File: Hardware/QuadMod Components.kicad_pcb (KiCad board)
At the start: 4 copper layers, 70.6 x 100 mm, 119 parts, among them J1 Conn_01x08_Pin, J2 Conn_01x08_Pin, J3 Conn_01x08_Pin, J4 Conn_01x08_Pin, J5 Eurorack_10_pin_power, J6 USB_B_Micro, J7 Prog_Header, J8 Extra_Outs, U1 LD1117-3.3-4Tab, U2 STM32H563VIT, U3 TL072, U4 MCP6004, U5 TPS561201, U6 MCP6004, U7 MCP6002-xSN, U8 STF202-22T1G, U9 AK4619VN, Y1 8MHz 20pF

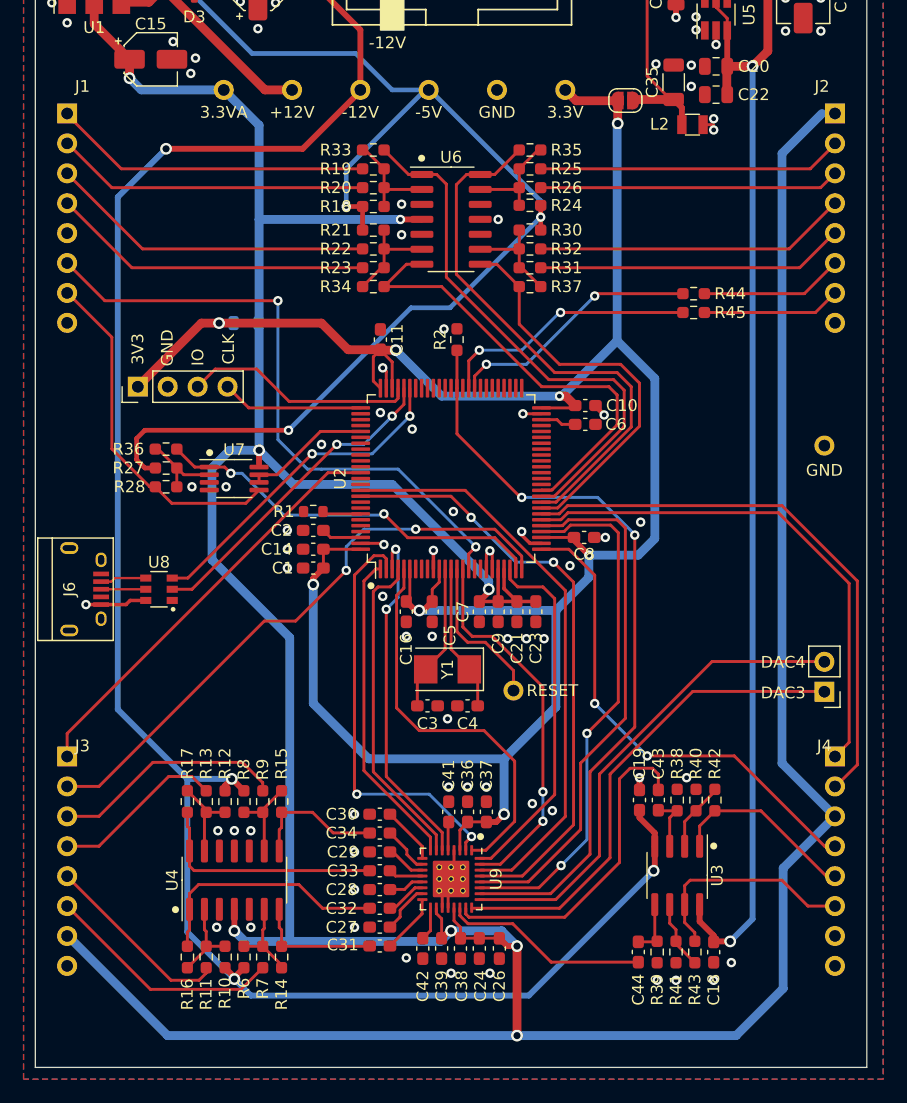
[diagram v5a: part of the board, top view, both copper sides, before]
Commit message: Started adding additional clock LED
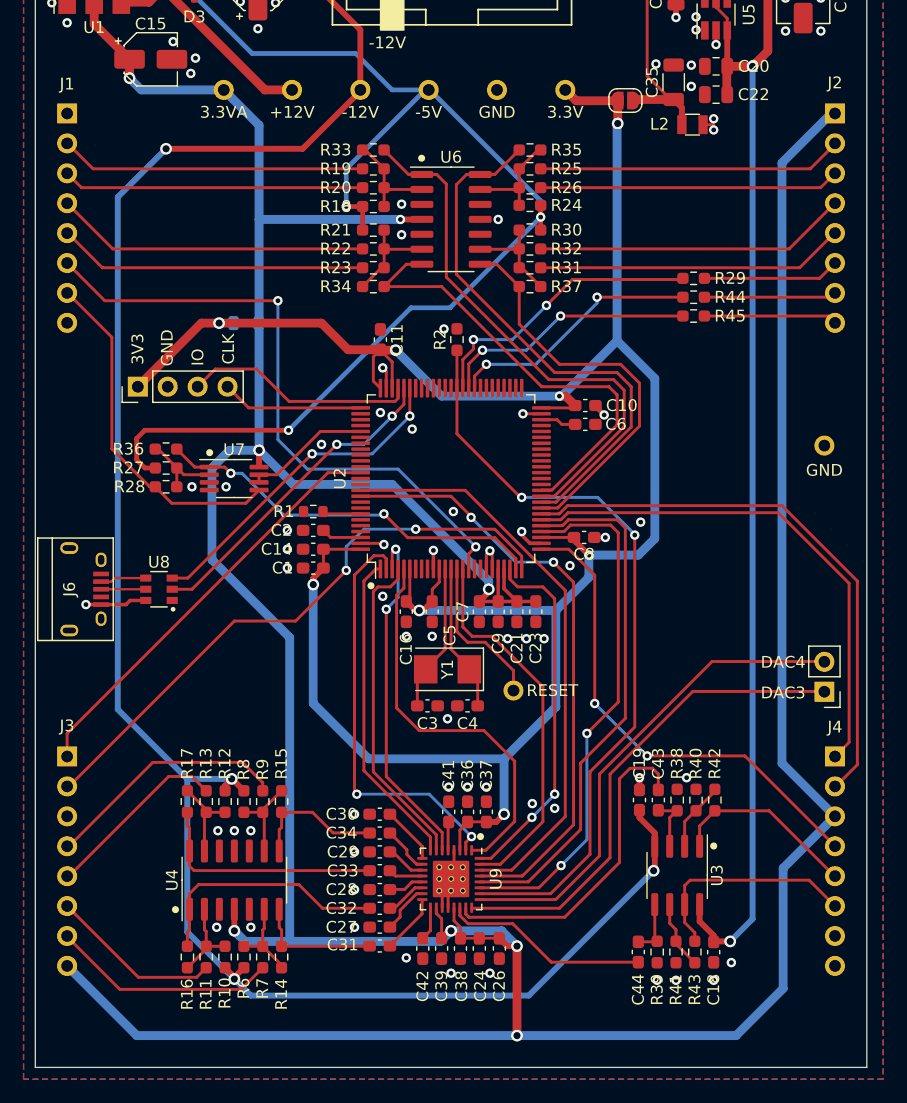
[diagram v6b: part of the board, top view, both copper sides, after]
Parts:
- added R29: 1k, Resistor_SMD:R_0603_1608Metric_Pad0.98x0.95mm_HandSolder, F.Cu at (155.9, 83.0)
- moved R44 0.30 mm to (155.9, 84.6)
- moved R45 0.30 mm to (155.9, 86.2)
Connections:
- J1 pad 1: /LFO_BASEFREQ_CV -> GND
- J1 pad 2: /LFO_BASEFREQ_POT -> /LFO_BASEFREQ_CV
- J1 pad 3: /DLY_FILTER_CV -> /LFO_BASEFREQ_POT
- J1 pad 4: /DLY_FILTER_POT -> /DLY_FILTER_CV
- J1 pad 5: GND -> /DLY_FILTER_POT
- J2 pad 1: +3.3VA -> GND
- J2 pad 6: /DELAY_LED -> /CLOCKED_LED
- J2 pad 7: /FX_LED -> /DELAY_LED
- J2 pad 8: GND -> /FX_LED
- J3 pad 3: /IN4 -> GND
- J3 pad 4: /IN3 -> /IN4
- J3 pad 5: /IN2 -> /IN3
- J3 pad 6: /IN1 -> /IN2
- J3 pad 7: +3.3VA -> /IN1
- J3 pad 8: GND -> +3.3VA
- U2 pad 61: unconnected-(U2-PD14-Pad61) -> /Clocked_Led_Out
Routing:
- net /Clocked_Led_Out: track 0.00 -> 24.4 mm, vias 0 -> 2
- net /CLOCKED_LED: track 0.00 -> 11.6 mm
- net /IN2: track 16.2 -> 14.7 mm
- net /LFO_BASEFREQ_CV: track 27.1 -> 26.0 mm
- net /DLY_FILTER_CV: track 27.8 -> 26.7 mm
- net /IN3: track 14.8 -> 15.8 mm
- net /LFO_BASEFREQ_POT: track 26.6 -> 25.6 mm
- net /IN4: track 19.9 -> 21.0 mm
- net /DLY_FILTER_POT: track 27.4 -> 26.3 mm
- net /IN1: track 20.3 -> 19.3 mm
- net /DELAY_LED: track 12.2 -> 11.2 mm
- net /SAI2_SD_B: vias 0 -> 2
- net /SAI2_SD_A: vias 2 -> 0

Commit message: Clean up of schematics and PCBS
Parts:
- added J9: Test_Outs, Connector_PinHeader_2.54mm:PinHeader_1x02_P2.54mm_Vertical, F.Cu at (104.1, 94.8)
- added TP9: TestPoint, Custom_Footprints:1mm_Test_Point, F.Cu at (102.7, 147.1)
- moved C15 2.00 mm to (109.8, 66.4), turned to -90 degrees
- moved J8 1.03 mm to (167.9, 118.6)
- moved R5 0.10 mm to (114.2, 53.5)
- moved C27 0.05 mm to (129.2, 138.1)
- moved C31 0.05 mm to (129.2, 139.7)
- moved C32 0.05 mm to (129.2, 136.5)
- moved C28 0.05 mm to (129.2, 134.9)
- moved C29 0.05 mm to (129.2, 131.7)
- moved C30 0.05 mm to (129.2, 128.5)
- moved C33 0.05 mm to (129.2, 133.3)
- moved C34 0.05 mm to (129.2, 130.1)
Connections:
- J4 pad 1: /LFO_RANGE -> GND
- J4 pad 2: /DLY_MIX -> /LFO_RANGE
- J4 pad 3: +3.3VA -> /DLY_MIX
- J4 pad 4: /FX_MIX -> +3.3VA
- J4 pad 5: /OUT_AMP2 -> /FX_MIX
- J4 pad 6: /OUT_AMP1 -> /OUT_AMP2
- J4 pad 7: GND -> /OUT_AMP1
- U2 pad 78: unconnected-(U2-PC10-Pad78) -> /Test_Out1
- U2 pad 79: unconnected-(U2-PC11-Pad79) -> /Test_Out2
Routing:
- net +3.3VA: track 345.2 -> 278.1 mm, vias 21 -> 20
- net /Test_Out2: track 0.00 -> 24.3 mm
- net /Test_Out1: track 0.00 -> 23.6 mm
- net /DLY_TIME_CV: track 29.7 -> 34.8 mm
- net /LFO_RANGE: track 44.1 -> 46.8 mm
- net /DLY_MIX: track 48.0 -> 50.6 mm
- net /OUT_AMP2: track 16.0 -> 17.1 mm
- net /OUT_AMP1: track 18.9 -> 20.0 mm
- net /FX_MIX: track 41.8 -> 42.8 mm
- net /Audio_Out4: track 41.7 -> 42.4 mm
- net /Audio_Out2: track 27.9 -> 28.6 mm
- net /Audio_Out3: track 41.7 -> 42.4 mm
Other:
- board text added: "1"
- board text added: "2"
- board text added: "QuadMod Components v1.0 Mountjoy Modular 2024"

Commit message: Draft Gerber Creation
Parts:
- moved R11 0.70 mm to (113.8, 140.6)
- moved R13 0.70 mm to (113.8, 127.4)
- moved R14 0.70 mm to (120.2, 140.6)
- moved R15 0.70 mm to (120.2, 127.4)
- moved R16 0.70 mm to (112.2, 140.6)
- moved R17 0.70 mm to (112.2, 127.4)
- moved R6 0.70 mm to (117.0, 140.6)
- moved R7 0.70 mm to (118.6, 140.6)
- moved R8 0.70 mm to (117.0, 127.4)
- moved R9 0.70 mm to (118.6, 127.4)
- moved U4 0.70 mm to (116.2, 134.1)
- moved R10 0.70 mm to (115.4, 140.6)
- moved R12 0.70 mm to (115.4, 127.4)
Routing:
- net +3.3V: track 201.2 -> 202.5 mm
- net -12V: track 173.9 -> 173.1 mm
- net /IN4: track 21.0 -> 20.2 mm
- net /IN3: track 15.8 -> 15.1 mm
- net /IN2: track 14.7 -> 14.0 mm
- net /IN1: track 19.3 -> 18.6 mm
- net /Audio_In2: track 21.0 -> 21.7 mm
- net /Audio_In4: track 11.6 -> 12.3 mm
- net /Audio_In1: track 10.7 -> 11.3 mm
- net /Audio_In3: track 20.1 -> 20.8 mm
- net GND: vias 73 -> 196
